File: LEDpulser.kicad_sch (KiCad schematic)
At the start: 48 parts

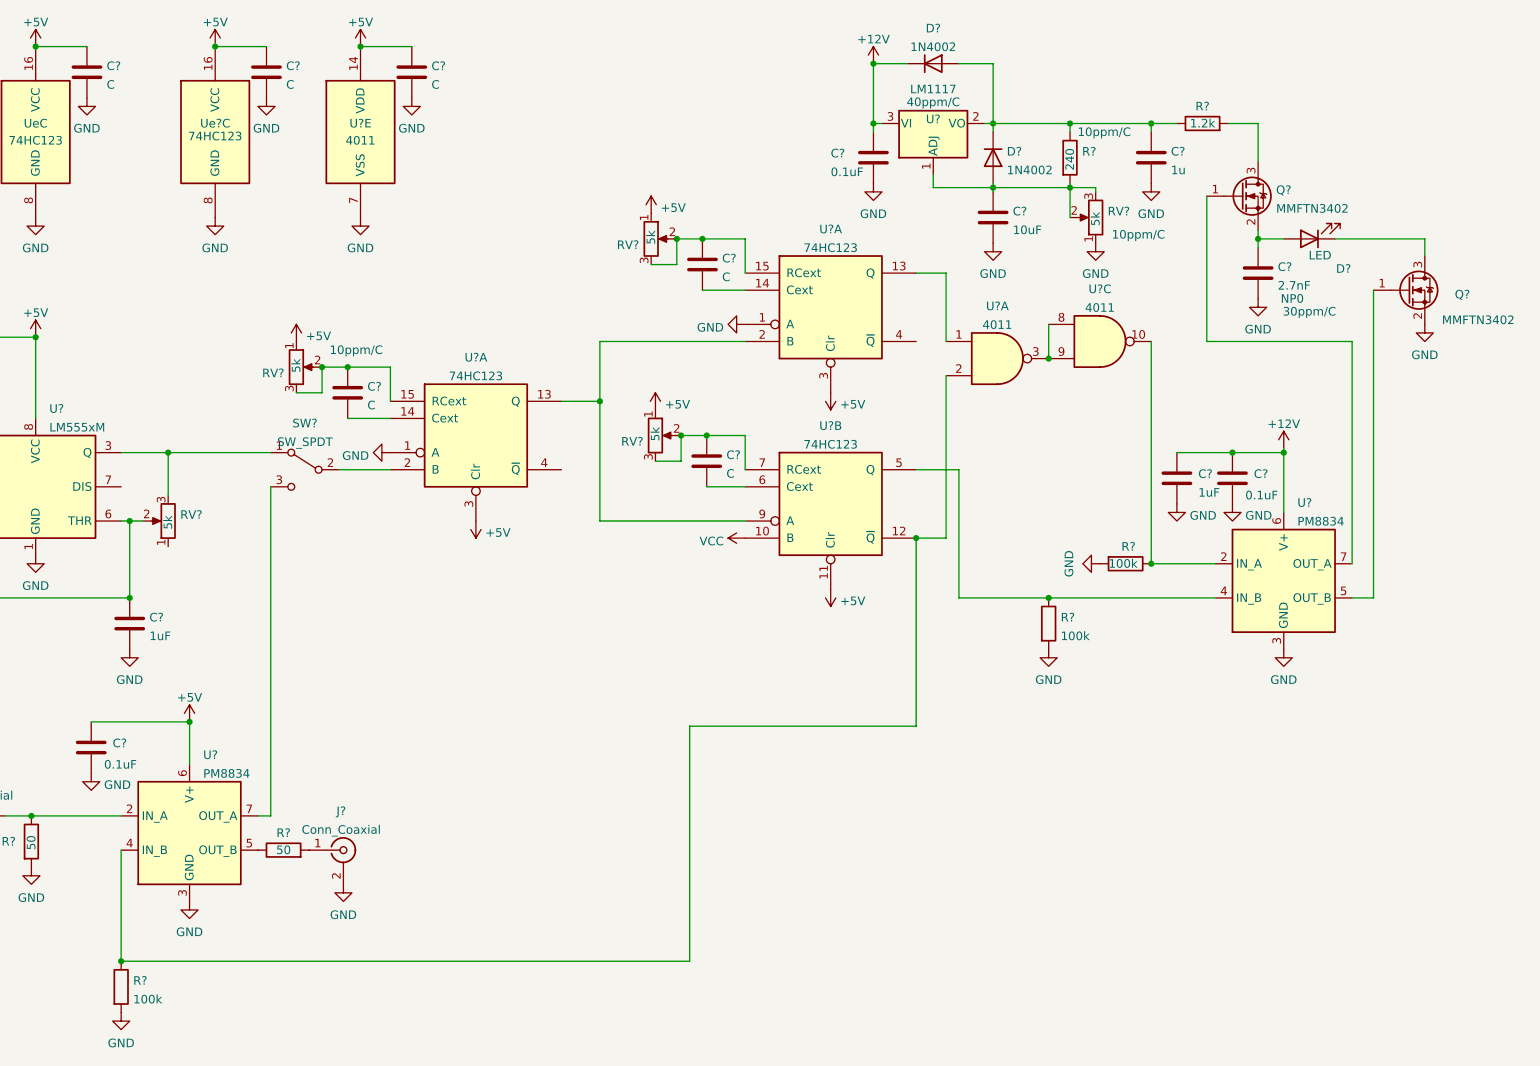
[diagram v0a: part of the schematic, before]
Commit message: Switched to P-channel charging FET and added LED short path.
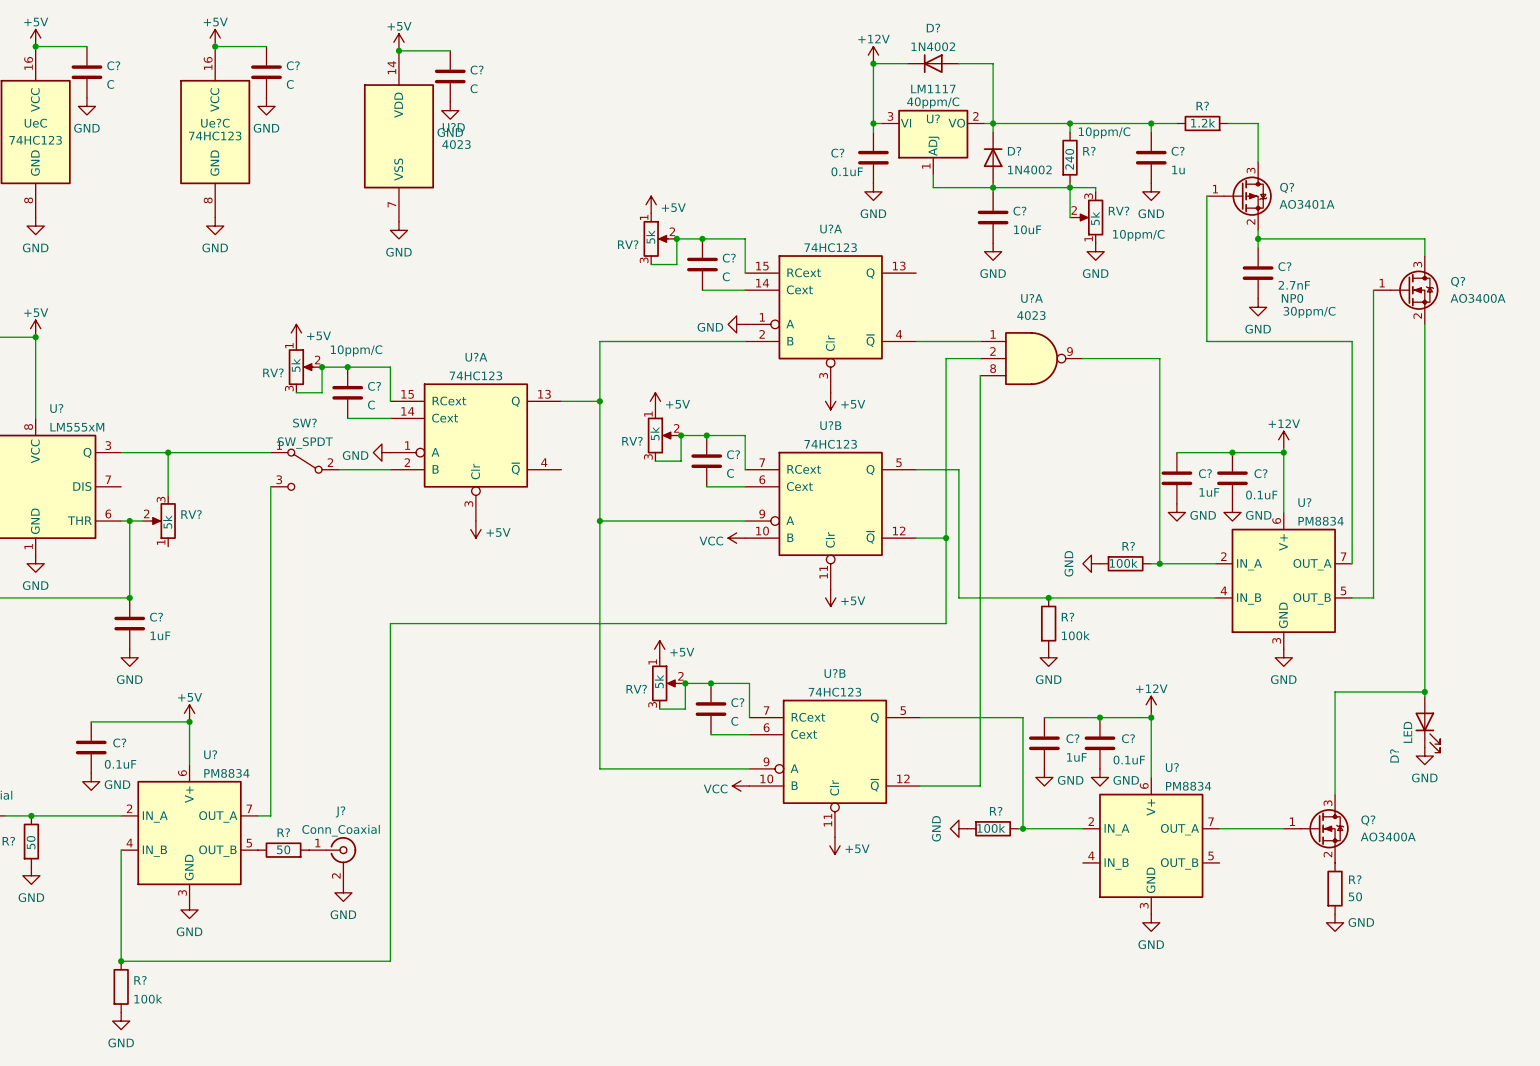
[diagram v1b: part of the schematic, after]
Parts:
- removed C?: C, symbol Device:C
- removed Q? (x2): MMFTN3402, Package_TO_SOT_SMD:SOT-23, symbol Transistor_FET:BSS138
- removed U? (x3): 4011, symbol 4xxx:4011
- added C? (x2): C, symbol Device:C
- added C?: 0.1uF, symbol Device:C
- added C?: 1uF, symbol Device:C
- added Q?: AO3401A, Package_TO_SOT_SMD:SOT-23, symbol Transistor_FET:AO3401A
- added Q? (x2): AO3400A, Package_TO_SOT_SMD:SOT-23, symbol Transistor_FET:AO3400A
- added R?: 100k, symbol Device:R
- added R?: 50, symbol Device:R
- added RV?: 5k, symbol Device:R_Potentiometer
- added U? (x2): 4023, symbol 4xxx:4023
- added U?: PM8834, symbol Driver_FET:EL7202CN
- added U?: 74HC123, symbol 74xx:74HC123
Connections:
- net +12V: now also C?.1, C?.1, U?.6 (V+)
- net +5V: now also C?.1, RV?.1, U?.11 (Clr), U?.14 (VDD)
- net GND: now also D?.1 (K), C?.2, C?.2, C?.2, R?.2, R?.2, U?.3 (GND), U?.7 (VSS)
- net VCC: now also U?.10 (B)
- net at U?.5 (OUT_B): now also Q?.1 (G)
- net at R?.1, U?.2 (IN_A): now also U?.9
- net at R?.1, U?.12 (~{Q}), U?.4 (IN_B): now also U?.2
- net at U?.13 (Q), U?.2 (B), U?.9 (A): now also U?.9 (A)
- net at U?.4 (~{Q}): now also U?.1
- net at C?.1: now also Q?.2 (S), Q?.3 (D); no longer D?.2 (A)
- net at R?.2: now also Q?.3 (D)
- net at U?.7 (OUT_A): now also Q?.1 (G)
- new net: U?.12 (~{Q}), U?.8
- new net: C?.1, RV?.2, RV?.3, U?.7 (RCext)
- new net: R?.1, U?.2 (IN_A), U?.5 (Q)
- new net: Q?.1 (G), U?.7 (OUT_A)
- new net: C?.2, U?.6 (Cext)
- new net: Q?.2 (S), R?.1
- new net: D?.2 (A), Q?.2 (S), Q?.3 (D)
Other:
- moved on the sheet: D?

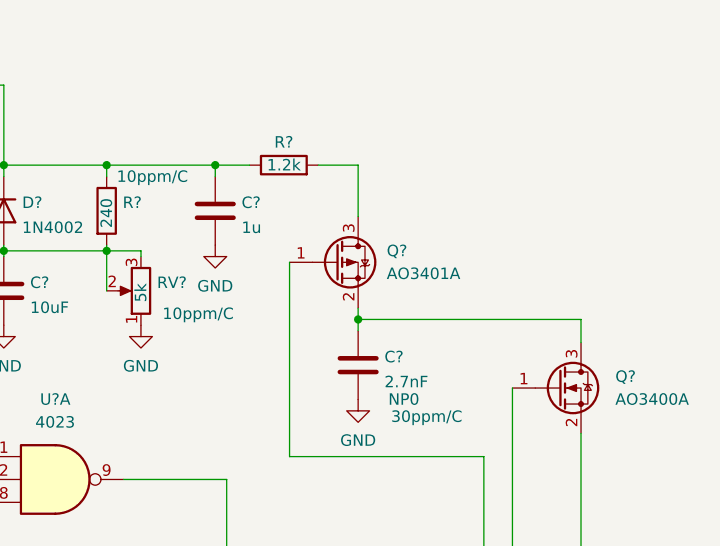
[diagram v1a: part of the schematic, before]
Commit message: Removed pmosfet from simulation, it was causing issues and was unimportant. Switched GS leads on pmosfet to proper biasing.
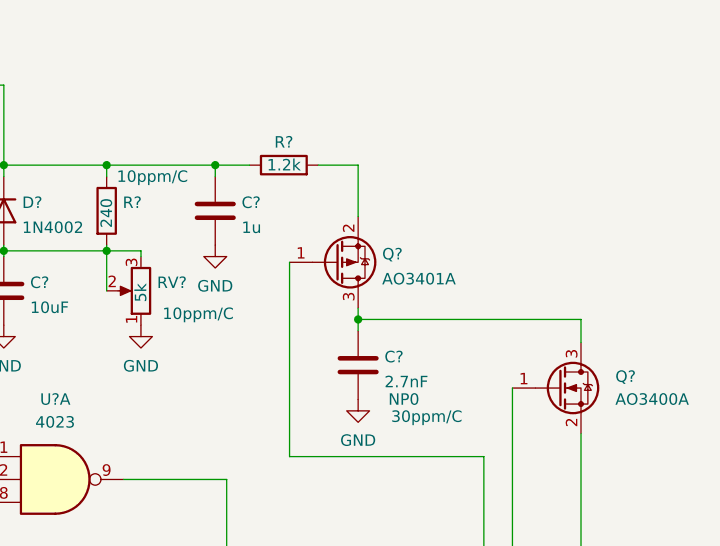
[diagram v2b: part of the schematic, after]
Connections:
- net at C?.1, Q?.3 (D): now also Q?.3 (D); no longer Q?.2 (S)
- net at R?.2: now also Q?.2 (S); no longer Q?.3 (D)
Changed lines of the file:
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@@
     (pin "1")
   )
-  (symbol (lib_id "Transistor_FET:AO3401A") (at 239.395 67.31 0) (unit 1)
+  (symbol (lib_id "Transistor_FET:AO3401A") (at 239.395 67.31 0) (mirror x) (unit 1)
     (in_bom yes) (on_board yes) (fields_autoplaced)
-    (property "Reference" "Q?" (id 0) (at 245.11 66.0399 0)
+    (property "Reference" "Q?" (id 0) (at 244.602 66.4015 0)
       (effects (font (size 1.27 1.27)) (justify left))
     )
-    (property "Value" "AO3401A" (id 1) (at 245.11 68.5799 0)
+    (property "Value" "AO3401A" (id 1) (at 244.602 69.1766 0)
       (effects (font (size 1.27 1.27)) (justify left))
     )
-    (property "Footprint" "Package_TO_SOT_SMD:SOT-23" (id 2) (at 244.475 69.215 0)
+    (property "Footprint" "Package_TO_SOT_SMD:SOT-23" (id 2) (at 244.475 65.405 0)
       (effects (font (size 1.27 1.27) italic) (justify left) hide)
     )

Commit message: Fixed capacitor discharge timing in schematic. Added timing to manual.
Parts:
- removed C?: 0.1uF, symbol Device:C
- removed R?: 100k, symbol Device:R
- added C1, C22: 0.1uF, Capacitor_SMD:C_0603_1608Metric, symbol Device:C
- added C20: C, Capacitor_SMD:C_0603_1608Metric, symbol Device:C
- added C21: 1uF, Capacitor_SMD:C_0603_1608Metric, symbol Device:C
- added J1: RJ45_Shielded, symbol Connector:RJ45_Shielded
- added R6, R7: 100k, symbol Device:R
- added RV7: 5k, symbol Device:R_Potentiometer
- added unit 3 of U3
- added unit 2 of U3
- C10, C12, C13, C14, C15, C16, C17, C18, C19, C5, C6, C7, C8, C9: renamed from C?; footprint (none) -> Capacitor_SMD:C_0603_1608Metric
- C11, C2, C3, C4: renamed from C?; value C -> 0.1uF; footprint (none) -> Capacitor_SMD:C_0603_1608Metric
- gave numbers to parts that had none: 33
- renumbered Ue to U1
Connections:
- net +12V: no longer C16.1, C17.1, U8.6 (V+)
- net +5V: now also C16.1, C17.1, U3.3 (Clr), U8.6 (V+), C1.1, C21.1, C22.1, RV7.1, U3.11 (Clr), U3.16 (VCC); no longer U3.11 (Clr)
- net GND: now also Q2.2 (S), Q3.2 (S), U2.9 (A), U3.1 (A), C1.2, C21.2, C22.2, J1.1, J1.3, J1.5, J1.7, J1.SH, R6.2, R7.2, U3.8 (GND), U3.9 (A); no longer D3.1 (K), R4.2
- net CAP_VOLTAGE: now reaches C6.1, D1.2 (A), D2.1 (K), R1.1, U5.2 (VO)
- net CAP_VOLTAGE: now also Q1.2 (S), J1.8; no longer R2.1
- net at U2.12 (~{Q}), U4.2: no longer R10.1, U9.4 (IN_B)
- net at U4.8: now also U3.12 (~{Q}); no longer U3.12 (~{Q})
- net SYNC: now reaches J3.1 (In), R9.2
- net at C19.1, RV6.2, RV6.3: now also U3.15 (RCext); no longer U3.7 (RCext)
- net INT: now reaches RV5.3, SW1.1 (A), U7.3 (Q)
- net EXT: now reaches J2.1 (In), R8.1, U9.2 (IN_A)
- net at R5.1, U6.4 (IN_B): no longer U2.5 (Q)
- net at U1.13 (Q), U2.2 (B): now also U3.2 (B); no longer U2.9 (A), U3.9 (A)
- net at U8.2 (IN_A): now also R10.1, U2.5 (Q), U9.4 (IN_B), R6.1; no longer U3.5 (Q)
- net at U8.4 (IN_B): now also R7.1, U3.5 (Q)
- net LED_SHORT: now reaches U8.5 (OUT_B)
- net LED_SHORT: now also Q3.1 (G), J1.2
- net LED_ON: now reaches U8.7 (OUT_A)
- net LED_ON: now also Q2.1 (G), J1.4; no longer Q3.1 (G)
- net at C19.2: now also U3.14 (Cext); no longer U3.6 (Cext)
- net CAP_CHARGE: now reaches Q1.1 (G), U6.7 (OUT_A)
- net CAP_CHARGE: now also J1.6
- net at R2.2: now also Q1.3 (D); no longer Q1.2 (S)
- net at R4.1: now also C12.1, D3.2 (A), R2.1; no longer Q3.2 (S)
- net at U6.5 (OUT_B): no longer Q2.1 (G)
- net at U1.4 (~{Q}): now also U2.10 (B)
- removed net VCC: U2.10 (B), U3.10 (B)
- new net: C20.1, RV7.2, RV7.3, U3.7 (RCext)
- new net: C20.2, U3.6 (Cext)
- new net: U3.10 (B), U3.4 (~{Q})
- new net: Q3.3 (D), R4.2
- new net: D3.1 (K), Q2.3 (D)
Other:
- moved on the sheet: C10, C11, C12, C13, C14, C15, C16, C17, C18, C19, C2, C3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

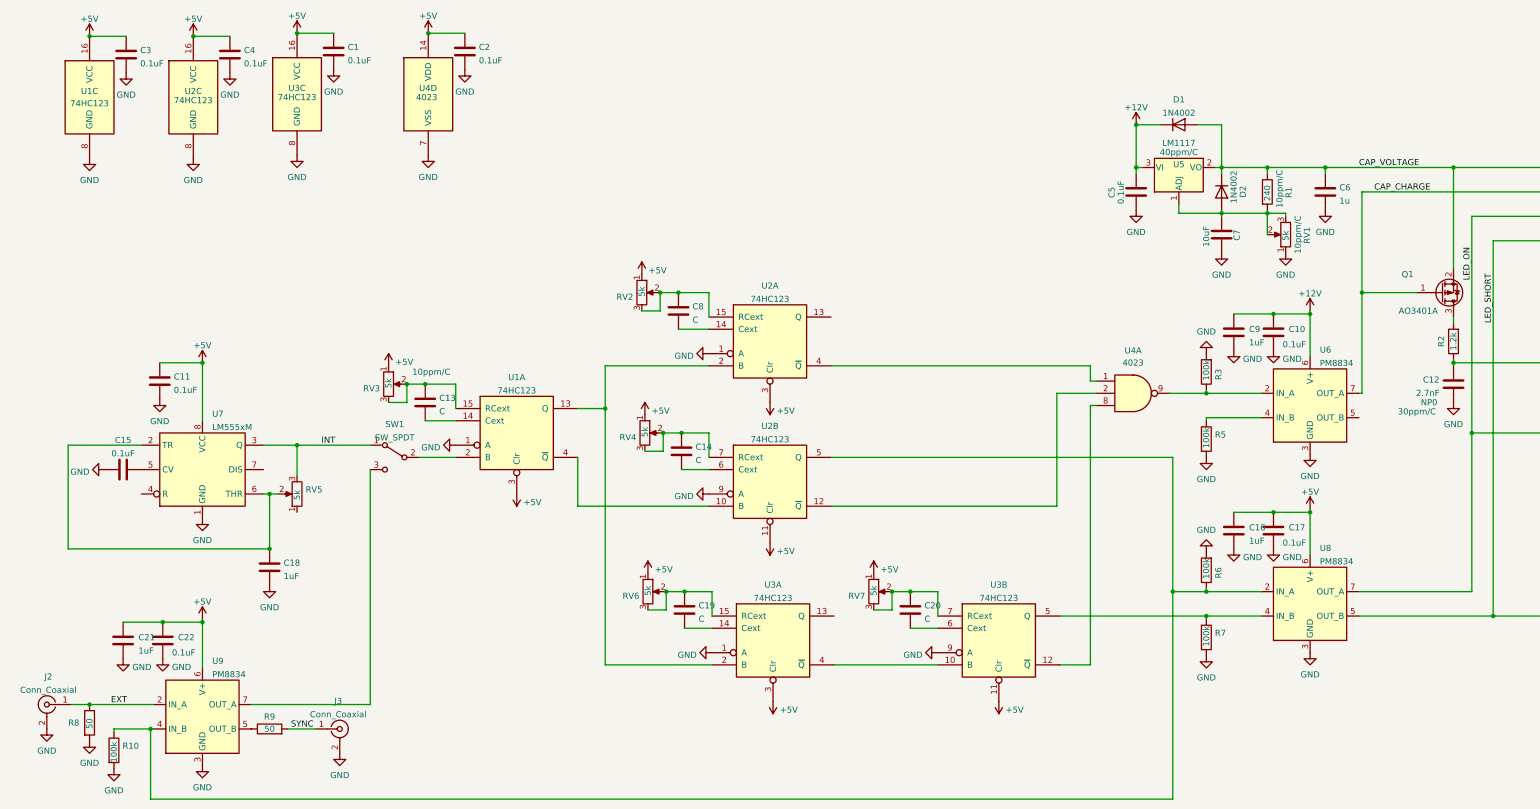
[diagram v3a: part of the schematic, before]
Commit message: Component selection on most components. Locked package selection.
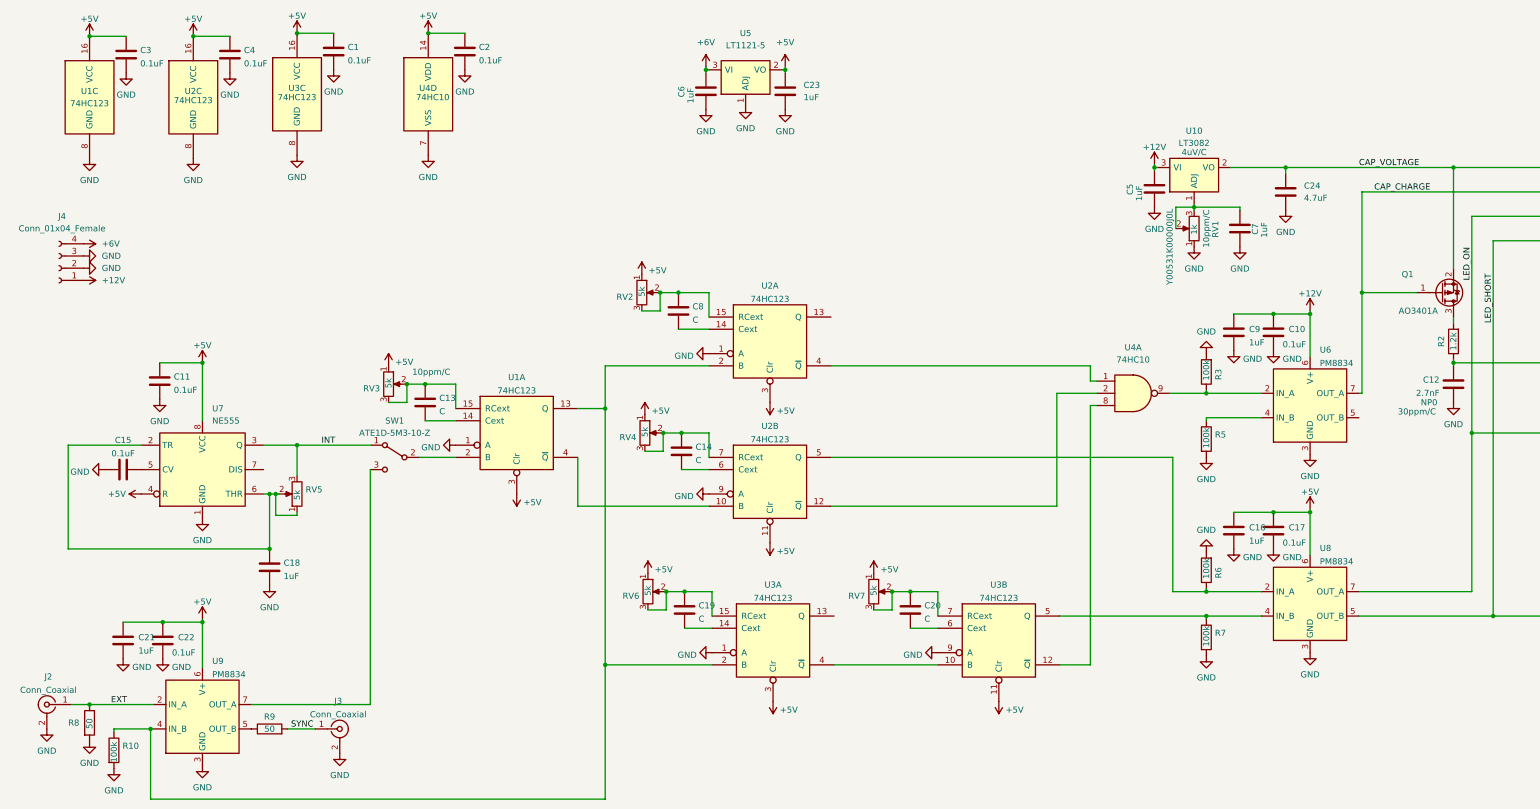
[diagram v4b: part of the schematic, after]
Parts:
- removed D1, D2: 1N4002, symbol Device:D
- removed R1: 240, symbol Device:R
- removed U5: LM1117, symbol Regulator_Linear:LM1117-ADJ
- added C23: 1uF, Capacitor_SMD:C_0603_1608Metric, symbol Device:C
- added C24: 4.7uF, Capacitor_SMD:C_0603_1608Metric, symbol Device:C
- added J4: Conn_01x04_Female, TerminalBlock_Phoenix:TerminalBlock_Phoenix_MKDS-1,5-4-5.08_1x04_P5.08mm_Horizontal, symbol Connector:Conn_01x04_Female
- added U10: LT3082, Package_TO_SOT_SMD:SOT-223-3_TabPin2, symbol Regulator_Linear:LT1117-ADJ
- added U5: LT1121-5, Package_TO_SOT_SMD:SOT-223-3_TabPin2, symbol Regulator_Linear:LT1117-ADJ
- C5: value 0.1uF -> 1uF
- C6: value 1u -> 1uF
- C7: value 10uF -> 1uF
- D3: footprint (none) -> LED_THT:LED_D3.0mm
- J1: footprint (none) -> Connector_RJ:RJ45_Amphenol_RJHSE538X
- J2, J3: footprint (none) -> Connector_Coaxial:BNC_TEConnectivity_1478035_Horizontal
- R10, R2, R3, R4, R5, R6, R7, R8, R9: footprint (none) -> Resistor_SMD:R_0603_1608Metric
- RV1: value 5k -> 1k; footprint (none) -> Potentiometer_THT:Potentiometer_Vishay_T73XX_Horizontal; Part# Y00535K00000J0L -> Y00531K00000J0L
- RV2, RV3, RV4, RV5, RV6, RV7: footprint (none) -> Potentiometer_THT:Potentiometer_Vishay_T73XX_Horizontal
- SW1: value SW_SPDT -> ATE1D-5M3-10-Z; footprint (none) -> Button_Switch_THT:SW_Lever_1P2T_NKK_GW12LxH
- U1, U2, U3: footprint (none) -> Package_SO:TSSOP-16_4.4x5mm_P0.65mm
- U4: value 4023 -> 74HC10; footprint (none) -> Package_SO:TSSOP-14_4.4x5mm_P0.65mm
- U6, U8, U9: footprint (none) -> Package_SO:SO-8_3.9x4.9mm_P1.27mm
- U7: value LM555xM -> NE555
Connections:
- net +12V: now also J4.1 (Pin_1), U10.3 (VI)
- net +5V: now also U7.4 (R), C23.1, U5.2 (VO)
- net CAP_VOLTAGE: now also C24.1, U10.2 (VO); no longer C6.1
- net GND: now also C23.2, C24.2, J4.2 (Pin_2), J4.3 (Pin_3), U5.1 (ADJ)
- net at C7.1, RV1.2, RV1.3: now also U10.1 (ADJ)
- net at RV5.1: now also C18.1, RV5.2, U7.2 (TR), U7.6 (THR)
- net at R6.1, U2.5 (Q), U8.2 (IN_A): no longer R10.1, U9.4 (IN_B)
- net at U1.13 (Q), U2.2 (B), U3.2 (B): now also R10.1, U9.4 (IN_B)
- new net +6V: C6.1, J4.4 (Pin_4), U5.3 (VI)
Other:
- moved on the sheet: C5, C7, RV1

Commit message: Component placement and initial hand routing.
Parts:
- C23, C24: Dielectric (none) -> NP0
- D3: footprint LED_THT:LED_D3.0mm -> Connector_Coaxial:BNC_Amphenol_B6252HB-NPP3G-50_Horizontal
- J2, J3: value Conn_Coaxial -> 0731375003; footprint Connector_Coaxial:BNC_TEConnectivity_1478035_Horizontal -> Connector_Coaxial:BNC_Amphenol_B6252HB-NPP3G-50_Horizontal
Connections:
- net INT: now also RV5.1; no longer RV5.3
- net at C18.1, RV5.2, U7.2 (TR)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: now also RV5.3; no longer RV5.1
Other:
- moved on the sheet: C12, J1, Q1, R2, RV5

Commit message: Routed first draft
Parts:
- removed D3: LED, Connector_Coaxial:BNC_Amphenol_B6252HB-NPP3G-50_Horizontal, symbol Device:LED
- added H1, H2: MountingHole, MountingHole:MountingHole_3.2mm_M3, symbol Mechanical:MountingHole
- added J5: LED, Connector:FanPinHeader_1x03_P2.54mm_Vertical, symbol Connector:Conn_Triaxial
- J2, J3: value 0731375003 -> EPS.00.250.NTN; footprint Connector_Coaxial:BNC_Amphenol_B6252HB-NPP3G-50_Horizontal -> Connector_Coaxial:SMA_Amphenol_132203-12_Horizontal
- RV1: footprint Potentiometer_THT:Potentiometer_Vishay_T73XX_Horizontal -> Potentiometer_THT:Potentiometer_Bourns_3266X_Horizontal
- RV2, RV3, RV4, RV6, RV7: value 5k -> 2k; footprint Potentiometer_THT:Potentiometer_Vishay_T73XX_Horizontal -> Potentiometer_THT:Potentiometer_Bourns_3266X_Horizontal; Part# Y00535K00000J0L -> 64XR2KLF; TemperatureCoefficient 10ppm/C -> (none)
- RV5: value 5k -> 1M; footprint Potentiometer_THT:Potentiometer_Vishay_T73XX_Horizontal -> Potentiometer_THT:Potentiometer_Bourns_3266X_Horizontal; Part# Y00535K00000J0L -> 3262X-1-105LF; TemperatureCoefficient 10ppm/C -> (none)
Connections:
- net GND: now also J5.3 (Ext)
- net LED_ON: no longer Q2.1 (G)
- net at C12.1, R2.1, R4.1: now also J5.2 (In2)
- net at Q2.3 (D): now also J5.1 (In1)
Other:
- moved on the sheet: Q2
